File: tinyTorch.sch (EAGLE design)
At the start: 29 parts, among them Q1 FDG6303N, U1 MCP1640, U2 ATtiny84A-SSU

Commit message: v1 as sent to fab.
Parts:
- D3, D4: MFR (none) -> Lite-On; MFR-PART-NO (none) -> LTL2H3EZ1K
- S1, S2: MFR (none) -> Omron; MFR-PART-NO (none) -> B3FS-1000
- U1: value MCP1640 -> MCP1640D
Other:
- note added: ""tinyTorch" by Jack Christensen is licensed under CC BY-SA 4.0 http://creativecommons.org/licenses/by-sa/4.0/"
- note added: "by Jack Christensen"
- note added: "tinyTorch"
- note added: "v1"
- note removed: "LED PWM Fire Effect by Jack Christensen is licensed under CC BY-SA 4.0 http://creativecommons.org/licenses/by-sa/4.0/"
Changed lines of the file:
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@@
 <grid distance="0.1" unitdist="inch" unit="inch" style="lines" multiple="1" display="no" altdistance="0.01" altunitdist="inch" altunit="inch"/>
 <layers>
-<layer number="1" name="Top" color="4" fill="1" visible="yes" active="no"/>
-<layer number="16" name="Bottom" color="1" fill="1" visible="yes" active="no"/>
-<layer number="17" name="Pads" color="2" fill="1" visible="yes" active="no"/>
-<layer number="18" name="Vias" color="2" fill="1" visible="yes" active="no"/>
-<layer number="19" name="Unrouted" color="6" fill="1" visible="yes" active="no"/>
-<layer number="20" name="Dimension" color="15" fill="1" visible="yes" active="no"/>
-<layer number="21" name="tPlace" color="7" fill="1" visible="yes" active="no"/>
-<layer number="22" name="bPlace" color="7" fill="1" visible="yes" active="no"/>
-<layer number="23" name="tOrigins" color="15" fill="1" visible="yes" active="no"/>
-<layer number="24" name="bOrigins" color="15" fill="1" visible="yes" active="no"/>
-<layer number="25" name="tNames" color="7" fill="1" visible="yes" active="no"/>
-<layer number="26" name="bNames" color="7" fill="1" visible="yes" active="no"/>
-<layer number="27" name="tValues" color="7" fill="1" visible="yes" active="no"/>
-<layer number="28" name="bValues" color="7" fill="1" visible="yes" active="no"/>
+<layer number="1" name="Top" color="4" fill="1" visible="no" active="no"/>
+<layer number="16" name="Bottom" color="1" fill="1" visible="no" active="no"/>
+<layer number="17" name="Pads" color="2" fill="1" visible="no" active="no"/>
+<layer number="18" name="Vias" color="2" fill="1" visible="no" active="no"/>
+<layer number="19" name="Unrouted" color="6" fill="1" visible="no" active="no"/>
+<layer number="20" name="Dimension" color="15" fill="1" visible="no" active="no"/>
+<layer number="21" name="tPlace" color="7" fill="1" visible="no" active="no"/>
+<layer number="22" name="bPlace" color="7" fill="1" visible="no" active="no"/>
+<layer number="23" name="tOrigins" color="15" fill="1" visible="no" active="no"/>
+<layer number="24" name="bOrigins" color="15" fill="1" visible="no" active="no"/>
+<layer number="25" name="tNames" color="7" fill="1" visible="no" active="no"/>
+<layer number="26" name="bNames" color="7" fill="1" visible="no" active="no"/>
+<layer number="27" name="tValues" color="7" fill="1" visible="no" active="no"/>
+<layer number="28" name="bValues" color="7" fill="1" visible="no" active="no"/>
 <layer number="29" name="tStop" color="7" fill="3" visible="no" active="no"/>
 <layer number="30" name="bStop" color="7" fill="6" visible="no" active="no"/>
@@
 <layer number="35" name="tGlue" color="7" fill="4" visible="no" active="no"/>
 <layer number="36" name="bGlue" color="7" fill="5" visible="no" active="no"/>
-<layer number="37" name="tTest" color="7" fill="1" visible="yes" active="no"/>
-<layer number="38" name="bTest" color="7" fill="1" visible="yes" active="no"/>
+<layer number="37" name="tTest" color="7" fill="1" visible="no" active="no"/>
+<layer number="38" name="bTest" color="7" fill="1" visible="no" active="no"/>
 <layer number="39" name="tKeepout" color="4" fill="11" visible="no" active="no"/>
 <layer number="40" name="bKeepout" color="1" fill="11" visible="no" active="no"/>
@@
 <layer number="44" name="Drills" color="7" fill="1" visible="no" active="no"/>
 <layer number="45" name="Holes" color="7" fill="1" visible="no" active="no"/>
-<layer number="46" name="Milling" color="3" fill="1" visible="yes" active="no"/>
-<layer number="47" name="Measures" color="7" fill="1" visible="yes" active="no"/>
-<layer number="48" name="Document" color="7" fill="1" visible="yes" active="no"/>
-<layer number="49" name="Reference" color="7" fill="1" visible="yes" active="no"/>
-<layer number="50" name="dxf" color="7" fill="1" visible="yes" active="no"/>
-<layer number="51" name="tDocu" color="7" fill="1" visible="yes" active="no"/>
-<layer number="52" name="bDocu" color="7" fill="1" visible="yes" active="no"/>
-<layer number="53" name="tGND_GNDA" color="7" fill="9" visible="yes" active="no"/>
-<layer number="54" name="bGND_GNDA" color="1" fill="9" visible="yes" active="no"/>
-<layer number="56" name="wert" color="7" fill="1" visible="yes" active="no"/>
+<layer number="46" name="Milling" color="3" fill="1" visible="no" active="no"/>
+<layer number="47" name="Measures" color="7" fill="1" visible="no" active="no"/>
+<layer number="48" name="Document" color="7" fill="1" visible="no" active="no"/>
+<layer number="49" name="Reference" color="7" fill="1" visible="no" active="no"/>
+<layer number="50" name="dxf" color="7" fill="1" visible="no" active="no"/>
+<layer number="51" name="tDocu" color="7" fill="1" visible="no" active="no"/>
+<layer number="52" name="bDocu" color="7" fill="1" visible="no" active="no"/>
+<layer number="53" name="tGND_GNDA" color="7" fill="9" visible="no" active="no"/>
+<layer number="54" name="bGND_GNDA" color="1" fill="9" visible="no" active="no"/>
+<layer number="56" name="wert" color="7" fill="1" visible="no" active="no"/>
 <layer number="91" name="Nets" color="2" fill="1" visible="yes" active="yes"/>
 <layer number="92" name="Busses" color="1" fill="1" visible="yes" active="yes"/>
@@
 <part name="R2" library="_jc" deviceset="R-US_" device="M0805" value="15"/>
 <part name="R3" library="_jc" deviceset="R-US_" device="M0805" value="65"/>
-<part name="U1" library="_jc" deviceset="MCP1640" device="" value="MCP1640"/>
+<part name="U1" library="_jc" deviceset="MCP1640" device="" value="MCP1640D"/>
 <part name="R6" library="_jc" deviceset="R-US_" device="M0805" value="976K"/>
 <part name="R5" library="_jc" deviceset="R-US_" device="M0805" value="562K"/>
@@
 <attribute name="MFR-PART-NO" value="C503D-WAN-CCBEB151"/>
 </part>
-<part name="D3" library="_jc" deviceset="LED" device="5MM-LONGPADS" value="Red"/>
-<part name="D4" library="_jc" deviceset="LED" device="5MM-LONGPADS" value="Red"/>
+<part name="D3" library="_jc" deviceset="LED" device="5MM-LONGPADS" value="Red">
+<attribute name="MFR" value="Lite-On"/>
+<attribute name="MFR-PART-NO" value="LTL2H3EZ1K"/>
+</part>
+<part name="D4" library="_jc" deviceset="LED" device="5MM-LONGPADS" value="Red">
+<attribute name="MFR" value="Lite-On"/>
+<attribute name="MFR-PART-NO" value="LTL2H3EZ1K"/>
+</part>
 <part name="R1" library="_jc" deviceset="R-US_" device="M0805" value="15"/>
 <part name="R4" library="_jc" deviceset="R-US_" device="M0805" value="65"/>
@@
 <part name="GND13" library="supply1" deviceset="GND" device=""/>
 <part name="GND14" library="supply1" deviceset="GND" device=""/>
-<part name="S1" library="_jc" deviceset="10-XX" device="SMT" value="DOWN/OFF"/>
-<part name="S2" library="_jc" deviceset="10-XX" device="SMT" value="UP/COLOR"/>
+<part name="S1" library="_jc" deviceset="10-XX" device="SMT" value="DOWN/OFF">
+<attribute name="MFR" value="Omron"/>
+<attribute name="MFR-PART-NO" value="B3FS-1000"/>
+</part>
+<part name="S2" library="_jc" deviceset="10-XX" device="SMT" value="UP/COLOR">
+<attribute name="MFR" value="Omron"/>
+<attribute name="MFR-PART-NO" value="B3FS-1000"/>
+</part>
 <part name="LOGO1" library="ohw-logo" deviceset="OSHW_LOGO_8MIL" device="X0150-NT" value="OSHW_LOGO_8MILX0150-NT"/>
 <part name="GND2" library="supply1" deviceset="GND" device=""/>
@@
 <sheet>
 <plain>
-<text x="17.78" y="5.08" size="2.54" layer="94" ratio="10">LED PWM Fire Effect by Jack Christensen is licensed
+<text x="17.78" y="5.08" size="2.54" layer="94" ratio="10">"tinyTorch" by Jack Christensen is licensed
 under CC BY-SA 4.0 http://creativecommons.org/licenses/by-sa/4.0/                       </text>
 <text x="17.78" y="15.24" size="3.81" layer="94" ratio="12">CC BY-SA</text>
+<text x="175.768" y="29.718" size="3.81" layer="94" ratio="12">tinyTorch</text>
+<text x="175.768" y="24.638" size="2.54" layer="94" ratio="12">by Jack Christensen</text>
+<text x="262.128" y="6.858" size="2.54" layer="94" ratio="12">v1</text>
 </plain>
 <instances>
@@
 <attribute name="NAME" x="54.356" y="127.508" size="1.778" layer="95" rot="R90"/>
 <attribute name="VALUE" x="53.975" y="135.128" size="1.778" layer="96" rot="R90"/>
+<attribute name="MFR" x="55.88" y="134.62" size="1.778" layer="96" display="off"/>
+<attribute name="MFR-PART-NO" x="55.88" y="134.62" size="1.778" layer="96" display="off"/>
 </instance>
 <instance part="D4" gate="G$1" x="63.5" y="134.62" smashed="yes">
 <attribute name="NAME" x="61.976" y="127.508" size="1.778" layer="95" rot="R90"/>
 <attribute name="VALUE" x="61.595" y="135.128" size="1.778" layer="96" rot="R90"/>
+<attribute name="MFR" x="63.5" y="134.62" size="1.778" layer="96" display="off"/>
+<attribute name="MFR-PART-NO" x="63.5" y="134.62" size="1.778" layer="96" display="off"/>
 </instance>
 <instance part="R1" gate="G$1" x="40.64" y="121.92" rot="R90"/>
@@
 <attribute name="VALUE" x="106.68" y="99.06" size="1.778" layer="96"/>
 </instance>
-<instance part="S1" gate="1" x="203.2" y="111.76"/>
-<instance part="S2" gate="1" x="190.5" y="111.76"/>
+<instance part="S1" gate="1" x="203.2" y="111.76">
+<attribute name="MFR" x="203.2" y="111.76" size="1.778" layer="96" display="off"/>
+<attribute name="MFR-PART-NO" x="203.2" y="111.76" size="1.778" layer="96" display="off"/>
+</instance>
+<instance part="S2" gate="1" x="190.5" y="111.76">
+<attribute name="MFR" x="190.5" y="111.76" size="1.778" layer="96" display="off"/>
+<attribute name="MFR-PART-NO" x="190.5" y="111.76" size="1.778" layer="96" display="off"/>
+</instance>
 <instance part="LOGO1" gate="G$1" x="55.88" y="17.78"/>
 <instance part="GND2" gate="1" x="203.2" y="101.6" smashed="yes">

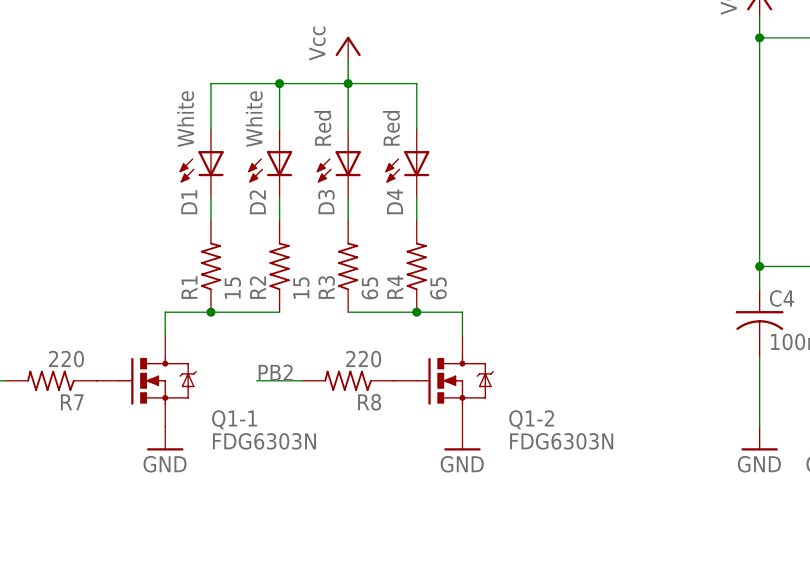
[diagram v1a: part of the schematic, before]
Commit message: Tweak resistor values.
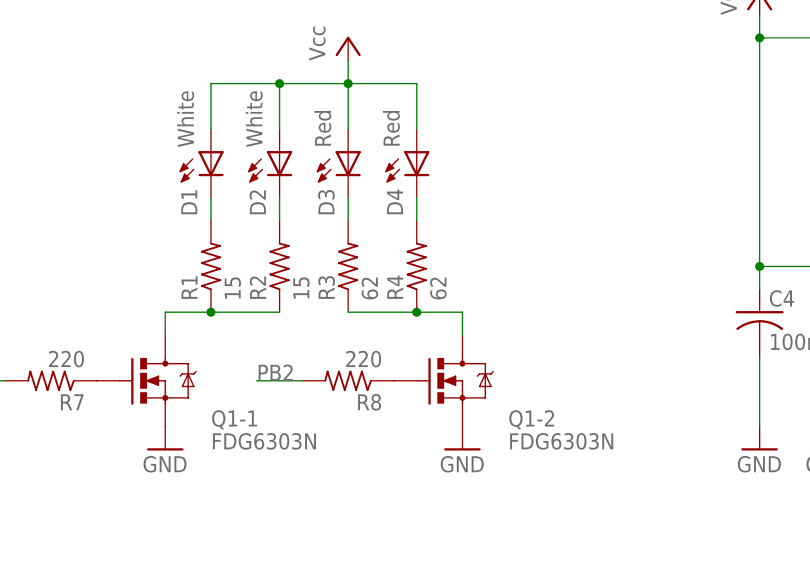
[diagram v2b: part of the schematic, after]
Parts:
- R3, R4: value 65 -> 62
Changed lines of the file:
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@@
 <part name="GND1" library="supply1" deviceset="GND" device=""/>
 <part name="R2" library="_jc" deviceset="R-US_" device="M0805" value="15"/>
-<part name="R3" library="_jc" deviceset="R-US_" device="M0805" value="65"/>
+<part name="R3" library="_jc" deviceset="R-US_" device="M0805" value="62"/>
 <part name="U1" library="_jc" deviceset="MCP1640" device="" value="MCP1640D"/>
 <part name="R6" library="_jc" deviceset="R-US_" device="M0805" value="976K"/>
@@
 </part>
 <part name="R1" library="_jc" deviceset="R-US_" device="M0805" value="15"/>
-<part name="R4" library="_jc" deviceset="R-US_" device="M0805" value="65"/>
+<part name="R4" library="_jc" deviceset="R-US_" device="M0805" value="62"/>
 <part name="P+1" library="supply1" deviceset="VCC" device="" value="Vcc"/>
 <part name="B1" library="_jc" deviceset="BATTERY-2AA" device="NOHOLES" value="2xAA">

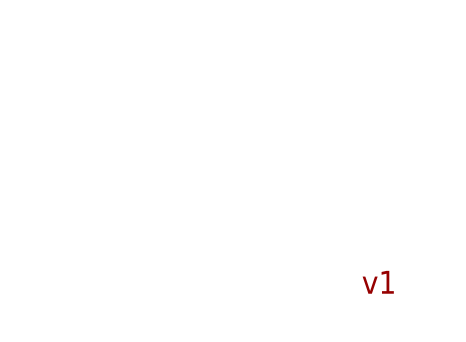
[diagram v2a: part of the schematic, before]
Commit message: Minor board layout tweaks.
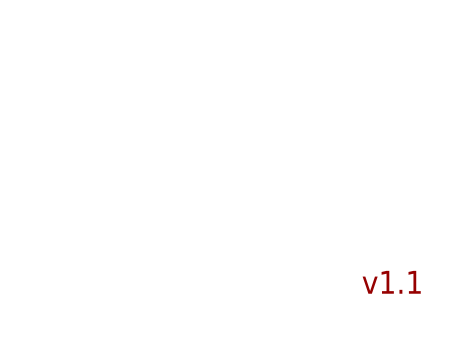
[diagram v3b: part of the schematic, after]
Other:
- note added: "v1.1"
- note removed: "v1"
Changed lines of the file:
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@@
 <text x="175.768" y="29.718" size="3.81" layer="94" ratio="12">tinyTorch</text>
 <text x="175.768" y="24.638" size="2.54" layer="94" ratio="12">by Jack Christensen</text>
-<text x="262.128" y="6.858" size="2.54" layer="94" ratio="12">v1</text>
+<text x="262.128" y="6.858" size="2.54" layer="94" ratio="12">v1.1</text>
 </plain>
 <instances>
